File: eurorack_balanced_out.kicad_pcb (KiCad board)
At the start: 2 copper layers, 22 parts, among them J1 Conn_02x05_Odd_Even, J2 AudioJack2_SwitchT, J3 AudioJack2_SwitchT, J4 AudioJack3, J5 AudioJack3, U1 TL072, U2 THAT1646S08, U3 THAT1646S08

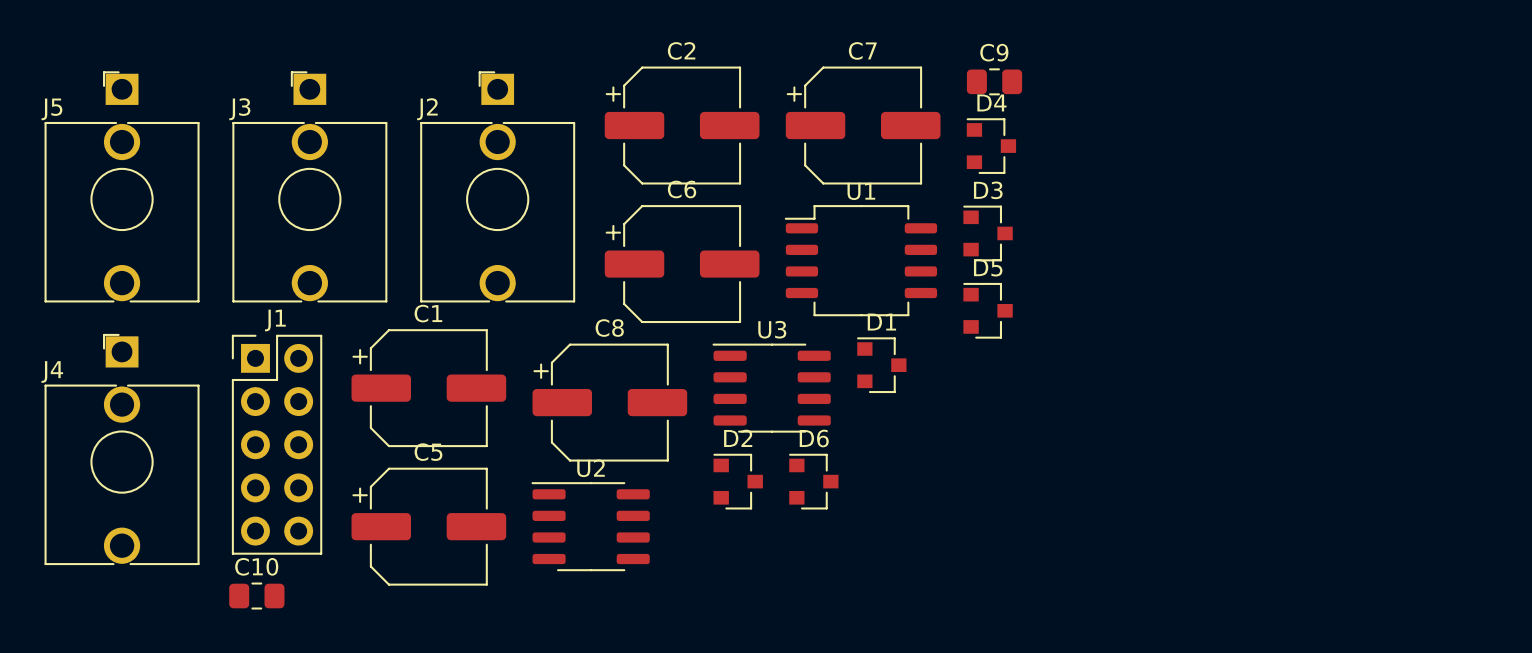
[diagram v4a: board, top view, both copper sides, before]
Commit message: use thonkycon TRS footprint for outputs
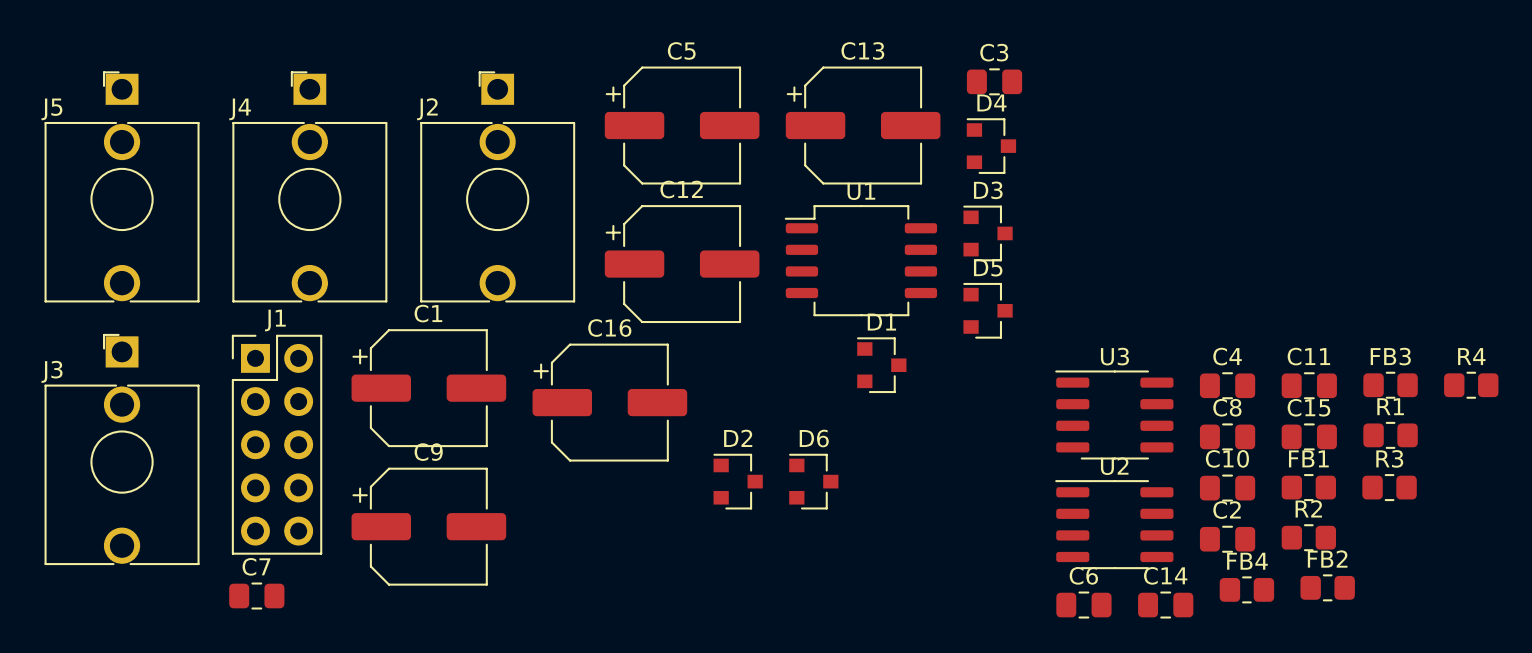
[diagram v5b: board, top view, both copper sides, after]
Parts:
- added C10: 100p, Capacitor_SMD:C_0805_2012Metric_Pad1.18x1.45mm_HandSolder, F.Cu at (137.2, 103.7)
- added C11: 100p, Capacitor_SMD:C_0805_2012Metric_Pad1.18x1.45mm_HandSolder, F.Cu at (142.0, 97.7)
- added C14: 100p, Capacitor_SMD:C_0805_2012Metric_Pad1.18x1.45mm_HandSolder, F.Cu at (133.5, 110.5)
- added C15: 100p, Capacitor_SMD:C_0805_2012Metric_Pad1.18x1.45mm_HandSolder, F.Cu at (142.0, 100.7)
- added C2: 100n, Capacitor_SMD:C_0805_2012Metric_Pad1.18x1.45mm_HandSolder, F.Cu at (137.2, 106.7)
- added C4: 100n, Capacitor_SMD:C_0805_2012Metric_Pad1.18x1.45mm_HandSolder, F.Cu at (137.2, 97.7)
- added C6: 100n, Capacitor_SMD:C_0805_2012Metric_Pad1.18x1.45mm_HandSolder, F.Cu at (128.7, 110.5)
- added C8: 100n, Capacitor_SMD:C_0805_2012Metric_Pad1.18x1.45mm_HandSolder, F.Cu at (137.2, 100.7)
- added FB1: 600R @ 100Mhz, Resistor_SMD:R_0805_2012Metric_Pad1.20x1.40mm_HandSolder, F.Cu at (141.9, 103.6)
- added FB2: 600R @ 100Mhz, Resistor_SMD:R_0805_2012Metric_Pad1.20x1.40mm_HandSolder, F.Cu at (143.1, 109.5)
- added FB3: 600R @ 100Mhz, Resistor_SMD:R_0805_2012Metric_Pad1.20x1.40mm_HandSolder, F.Cu at (146.8, 97.6)
- added FB4: 600R @ 100Mhz, Resistor_SMD:R_0805_2012Metric_Pad1.20x1.40mm_HandSolder, F.Cu at (138.3, 109.7)
- added R1: 39k, Resistor_SMD:R_0805_2012Metric_Pad1.20x1.40mm_HandSolder, F.Cu at (146.8, 100.6)
- added R2: 12k, Resistor_SMD:R_0805_2012Metric_Pad1.20x1.40mm_HandSolder, F.Cu at (141.9, 106.6)
- added R3: 39k, Resistor_SMD:R_0805_2012Metric_Pad1.20x1.40mm_HandSolder, F.Cu at (146.7, 103.6)
- added R4: 12k, Resistor_SMD:R_0805_2012Metric_Pad1.20x1.40mm_HandSolder, F.Cu at (151.5, 97.6)
- J1: value Conn_02x05_Odd_Even -> Eurorack_ribbon
- J2: value AudioJack2_SwitchT -> Audio_in_1
- J3: renamed from J4; value AudioJack3 -> Balanced_out_1; footprint Connector_Audio:Jack_3.5mm_QingPu_WQP-PJ398SM_Vertical_CircularHoles -> patchnut:Jack_3.5mm_ThonkiConn_TRS-PJ366ST_Vertical
- J4: renamed from J3; value AudioJack2_SwitchT -> Audio_in_2
- J5: value AudioJack3 -> Balanced_out_2; footprint Connector_Audio:Jack_3.5mm_QingPu_WQP-PJ398SM_Vertical_CircularHoles -> patchnut:Jack_3.5mm_ThonkiConn_TRS-PJ366ST_Vertical
- moved U2 30.8 mm to (130.5, 105.8)
- moved U3 20.2 mm to (130.5, 99.4)
- renumbered C6 to C12, C7 to C13, C8 to C16, C9 to C3, C2 to C5, C10 to C7, C5 to C9
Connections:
- net Net-(C5-Pad1) renamed Clamp_out_1_P
- net Net-(C6-Pad1) renamed Clamp_out_1_N
- net Net-(C7-Pad1) renamed Clamp_out_2_P
- net Net-(C8-Pad1) renamed Clamp_out_2_N
- net Net-(D1-Pad3) renamed Clamp_in_1
- net Net-(D2-Pad3) renamed Clamp_in_2

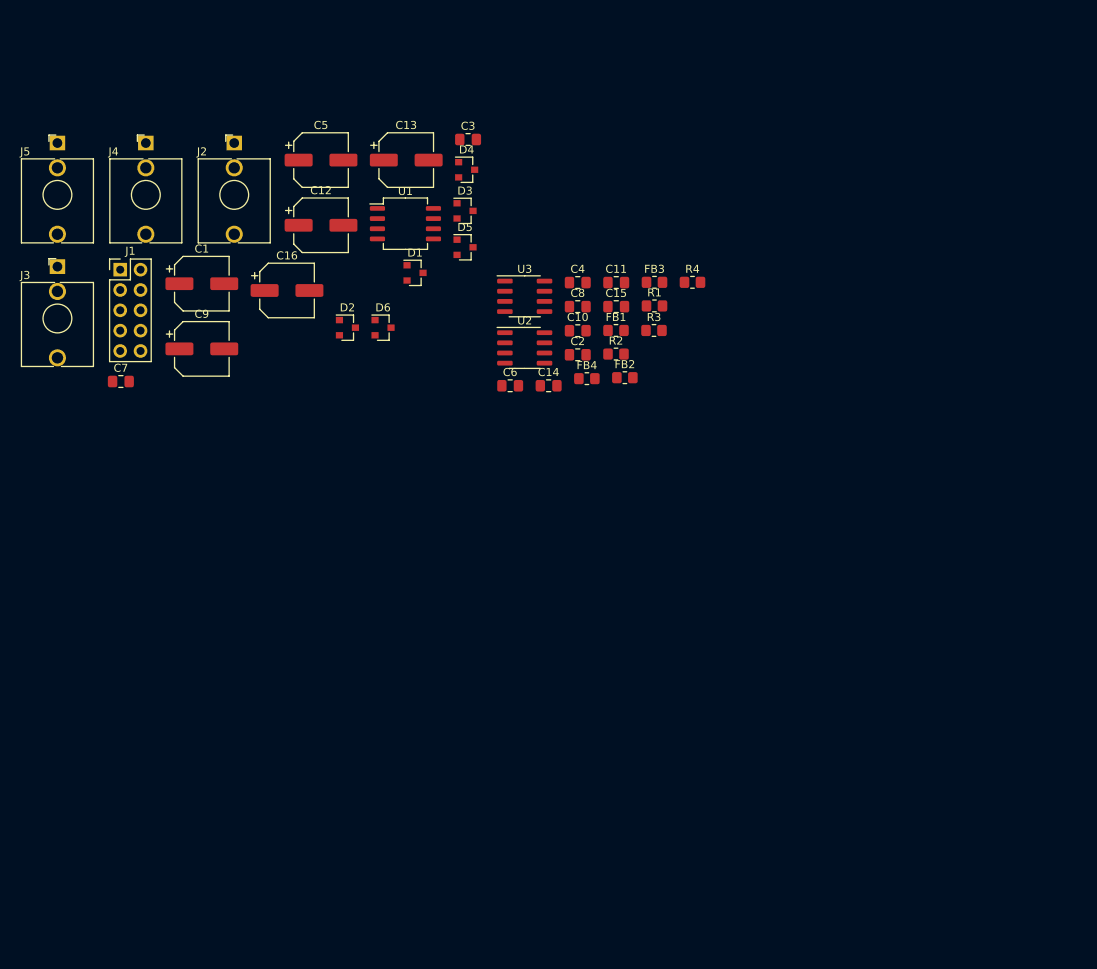
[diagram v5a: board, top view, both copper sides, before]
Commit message: add board outline and move components out of the way
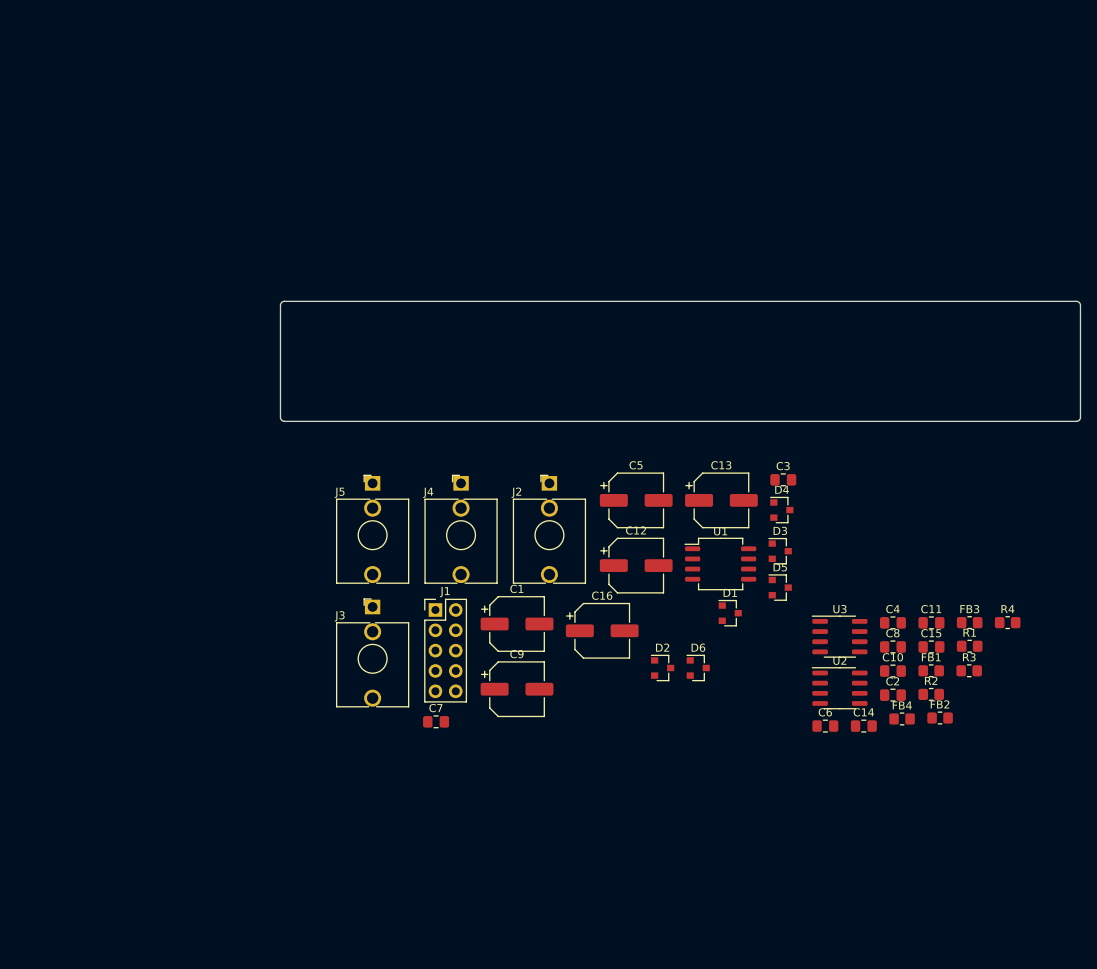
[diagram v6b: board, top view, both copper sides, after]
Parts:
- moved R1 58.0 mm to (186.2, 143.1)
- moved U2 58.0 mm to (169.9, 148.4)
- moved C10 58.0 mm to (176.6, 146.2)
- moved C12 58.0 mm to (144.5, 133.0)
- moved C16 58.0 mm to (140.2, 141.2)
- moved C6 58.0 mm to (168.1, 153.1)
- moved C7 58.0 mm to (119.5, 152.6)
- moved D2 58.0 mm to (147.8, 145.8)
- moved D5 58.0 mm to (162.5, 135.8)
- moved D6 58.0 mm to (152.2, 145.8)
- moved FB1 58.0 mm to (181.3, 146.2)
- moved J1 58.0 mm to (119.4, 138.6)
- moved J2 58.0 mm to (133.6, 122.8)
- moved R3 58.0 mm to (186.1, 146.2)
- moved U1 58.0 mm to (155.0, 132.8)
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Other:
- board outline added: 100 x 15 mm

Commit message: roughly place components
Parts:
- J2, J3, J4, J5: moved to B.Cu
- moved J5 83.8 mm to (194.8, 113.2)
- moved C9 71.8 mm to (178.2, 95.8)
- moved J4 62.7 mm to (184.5, 113.2)
- moved J1 39.8 mm to (102.5, 102.5)
- moved C12 38.8 mm to (170.5, 104.2), turned to 180 degrees
- moved C16 38.3 mm to (149.5, 104.0), turned to 180 degrees
- moved U2 36.9 mm to (170.5, 111.5)
- moved C1 36.7 mm to (126.2, 103.8)
- moved U3 33.7 mm to (156.0, 111.2)
- moved D6 33.4 mm to (124.2, 127.5)
- moved U1 31.0 mm to (136.8, 107.8)
- moved J2 26.6 mm to (108.8, 113.2)
- moved J3 26.0 mm to (119.0, 113.2)
- moved C5 22.8 mm to (126.2, 111.2), turned to 180 degrees
- moved C13 21.3 mm to (160.2, 104.2)
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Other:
- rule pad_to_mask_clearance: 0.051 -> 0.5

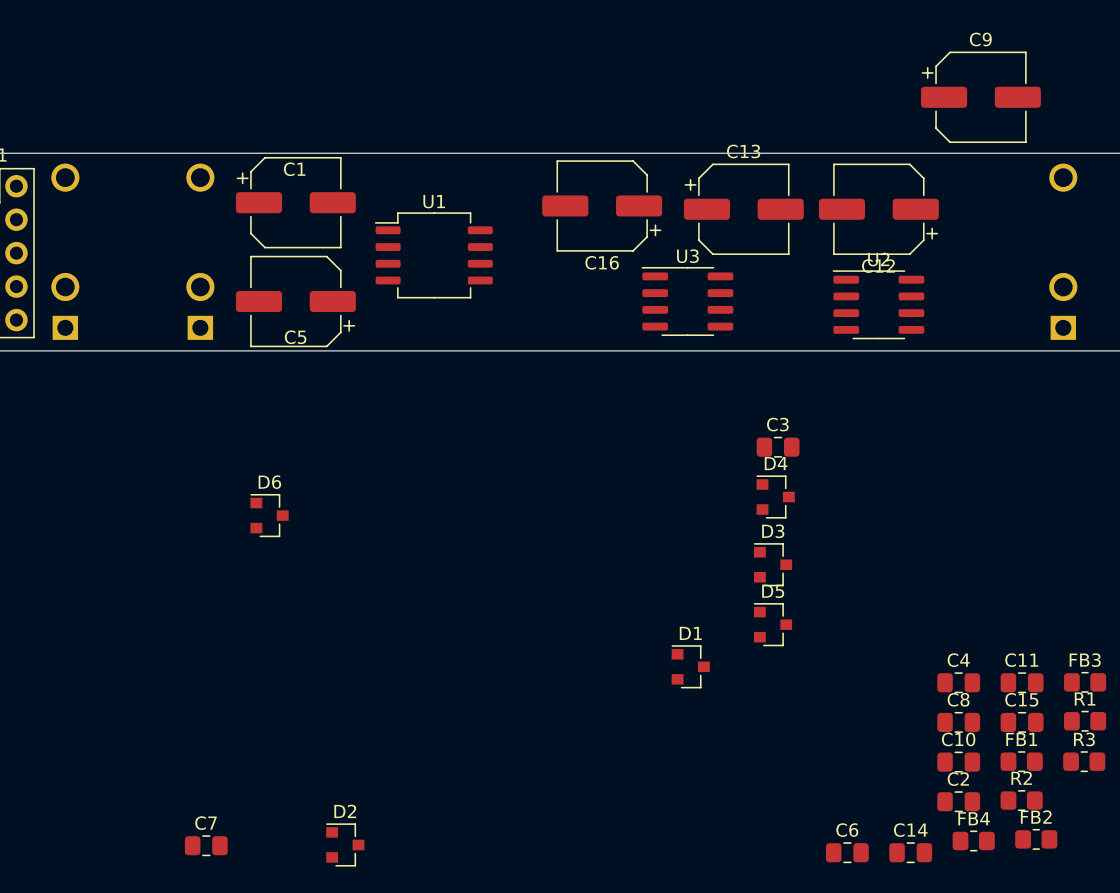
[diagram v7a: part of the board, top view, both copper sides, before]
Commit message: flip chips to back of the board
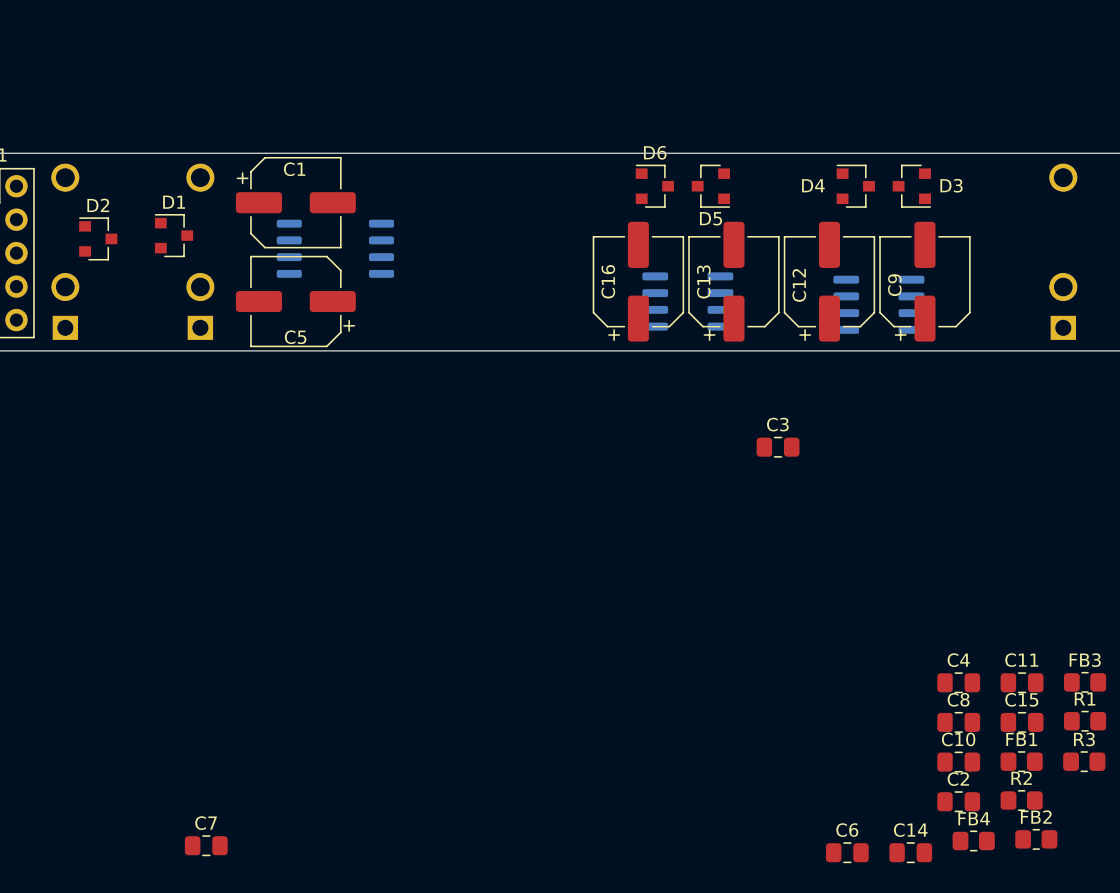
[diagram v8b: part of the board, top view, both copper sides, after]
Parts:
- U1, U2, U3: moved to B.Cu
- moved D1 51.1 mm to (117.0, 106.2)
- moved D2 49.7 mm to (111.2, 106.5)
- moved D6 38.5 mm to (153.5, 102.5)
- moved D5 33.6 mm to (157.8, 102.5), turned to 180 degrees
- moved D3 30.6 mm to (173.0, 102.5), turned to 180 degrees
- moved D4 24.4 mm to (168.8, 102.5)
- moved C9 14.6 mm to (174.0, 109.8), turned to 90 degrees
- moved U1 7.52 mm to (129.2, 107.2)
- moved C12 6.66 mm to (166.8, 109.8), turned to 90 degrees
- moved C16 6.37 mm to (152.2, 109.8), turned to 90 degrees
- moved C13 5.55 mm to (159.5, 109.8), turned to 90 degrees
